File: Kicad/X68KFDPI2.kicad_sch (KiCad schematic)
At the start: 29 parts, among them J1 HxC Connector, J11 Micro_SD_Card, J13 FD Int/Ext (0,1/2,3), J2 FD Ext Connector, J3 FD00, J4 FD01, J7 LedFD0, J8 LedFD1, J9 FloppyPWR, SW1 SW_Push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

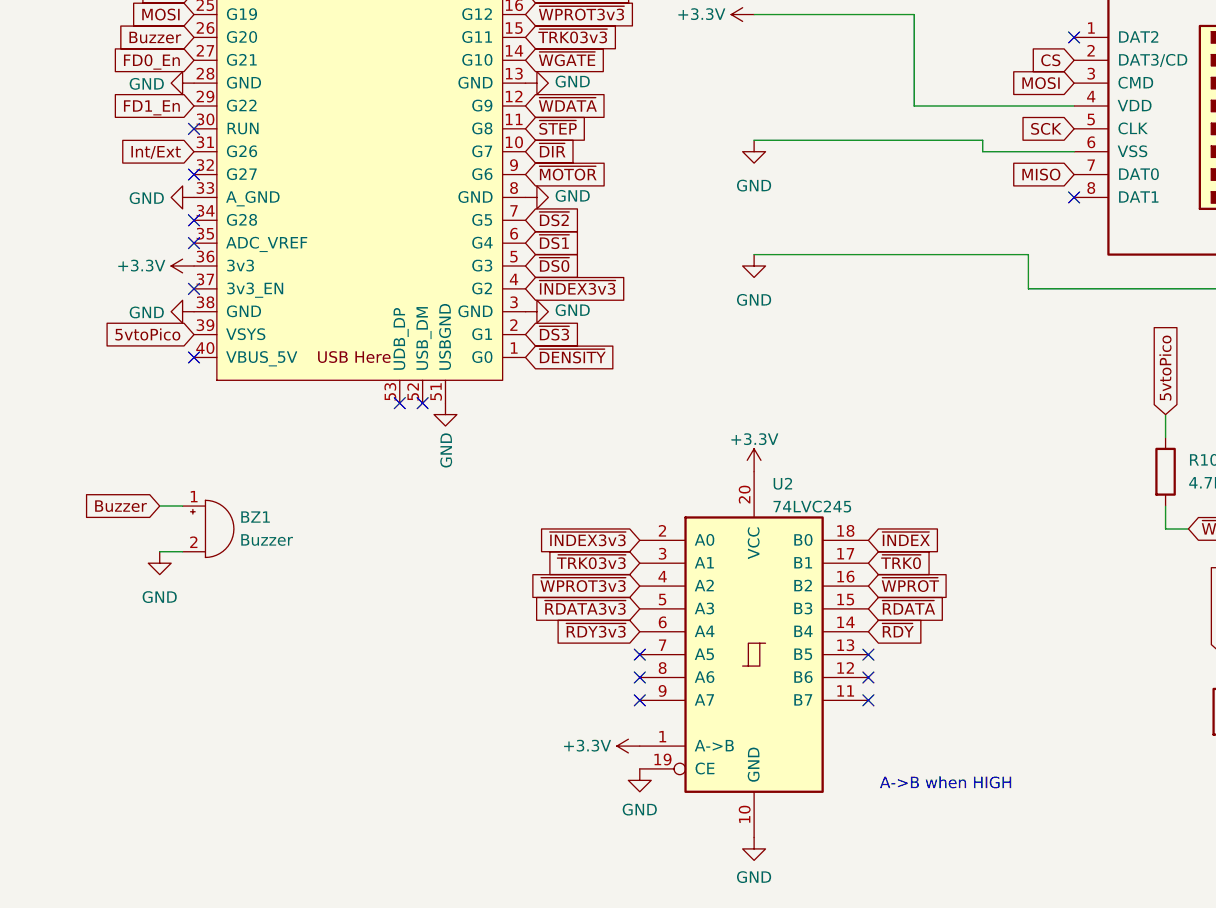
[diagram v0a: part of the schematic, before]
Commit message: Added 74lvc245 dir control
Test in progress for avoiding conflict when 2 x68kfdpi2w are used togheter
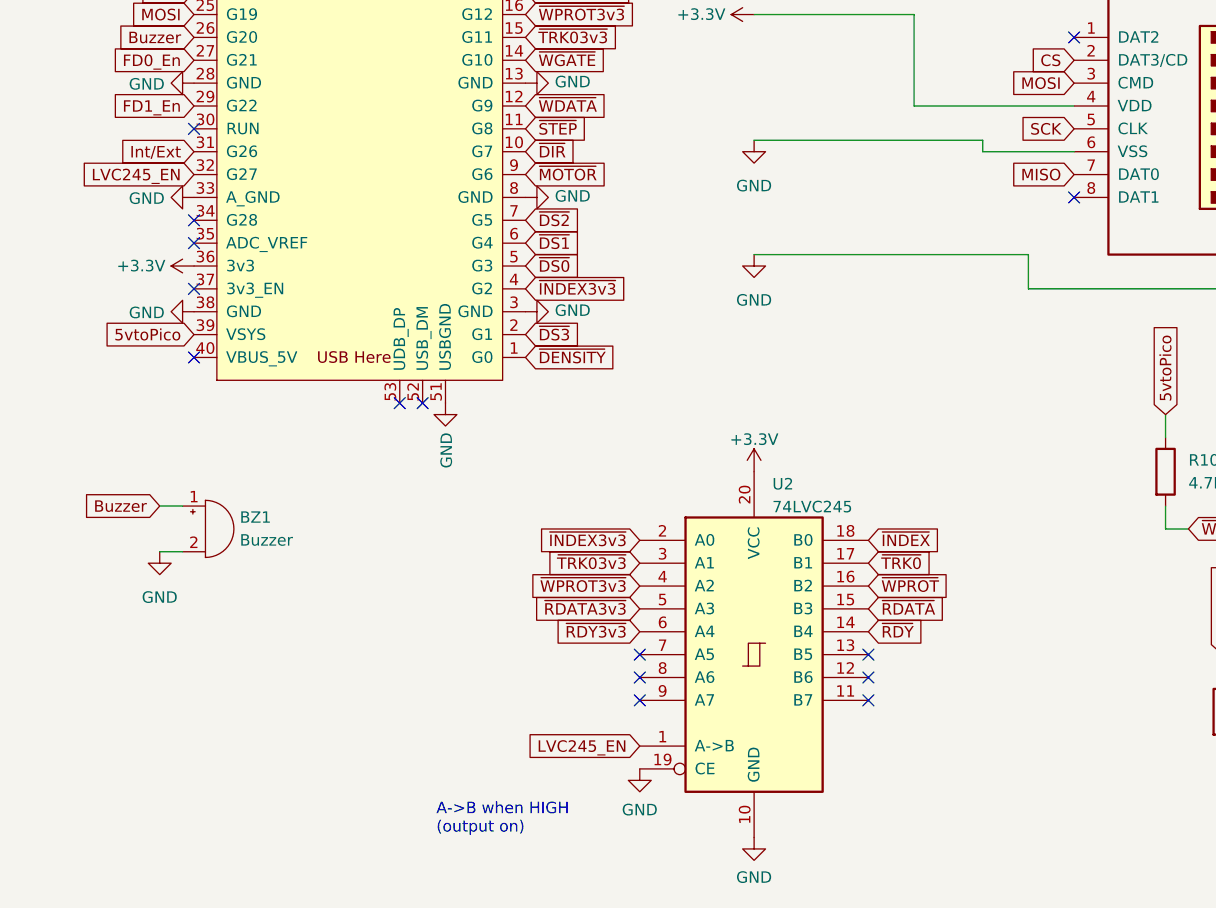
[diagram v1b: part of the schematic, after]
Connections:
- net +3.3V: no longer U2.1 (A->B)
- net LVC245_EN: now reaches RP1.32 (G27)
- net LVC245_EN: now also U2.1 (A->B)
- no-connect marks 31 -> 30
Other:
- note added: "A->B when HIGH (output on)"
- note removed: "A->B when HIGH"
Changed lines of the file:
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@@
 	(generator_version "9.0")
 	(paper "A4")
-	(text "A->B when HIGH"
+	(text "A->B when HIGH \n(output on)"
 		(exclude_from_sim no)
-		(at 105.41 177.8 0)
+		(at 56.134 182.626 0)
 		(effects
 			(font
@@
 	)
 	(no_connect
-		(at 29.21 109.22)
-	)
-	(no_connect
 		(at 29.21 104.14)
 	)
@@
 		)
 	)
+	(global_label "LVC245_EN"
+		(shape input)
+		(at 78.74 172.72 180)
+		(fields_autoplaced yes)
+		(effects
+			(font
+				(size 1.27 1.27)
+			)
+			(justify right)
+		)
+		(property "Intersheetrefs" "${INTERSHEET_REFS}"
+			(at 65.2925 172.72 0)
+			(effects
+				(font
+					(size 1.27 1.27)
+				)
+				(justify right)
+				(hide yes)
+			)
+		)
+	)
 	(global_label "~{MOTOR}"
 		(shape input)
@@
 		)
 	)
+	(global_label "LVC245_EN"
+		(shape input)
+		(at 29.21 109.22 180)
+		(fields_autoplaced yes)
+		(effects
+			(font
+				(size 1.27 1.27)
+			)
+			(justify right)
+		)
+		(property "Intersheetrefs" "${INTERSHEET_REFS}"
+			(at 15.7625 109.22 0)
+			(effects
+				(font
+					(size 1.27 1.27)
+				)
+				(justify right)
+				(hide yes)
+			)
+		)
+	)
 	(global_label "LEDFD0"
 		(shape input)
@@
 					(unit 1)
 				)
-			)
-		)
-	)
-	(symbol
-		(lib_id "power:+3.3V")
-		(at 78.74 172.72 90)
-		(unit 1)
-		(exclude_from_sim no)
-		(in_bom yes)
-		(on_board yes)
-		(dnp no)
-		(fields_autoplaced yes)
-		(property "Reference" "#PWR041"
-			(at 82.55 172.72 0)
-			(effects
-				(font
-					(size 1.27 1.27)
-				)
-				(hide yes)
-			)
-		)
-		(property "Value" "+3.3V"
-			(at 75.565 172.72 90)
-			(effects
-				(font
-					(size 1.27 1.27)
-				)
-				(justify left)
-			)
-		)
-		(property "Footprint" ""
-			(at 78.74 172.72 0)
-			(effects
-				(font
-					(size 1.27 1.27)
-				)
-				(hide yes)
-			)
-		)
-		(property "Datasheet" ""
-			(at 78.74 172.72 0)
-			(effects
-				(font
-					(size 1.27 1.27)
-				)
-				(hide yes)
-			)
-		)
-		(property "Description" "Power symbol creates a global label with name \"+3.3V\""
-			(at 78.74 172.72 0)
-			(effects
-				(font
-					(size 1.27 1.27)
-				)
-				(hide yes)
-			)
-		)
-		(pin "1"
-		)
-		(instances
-			(project "X68KFDPI2"
-				(path "/0f251f4d-18c3-4e16-8078-b8eaa683a5b6"
-					(reference "#PWR041")
-					(unit 1)
-				)

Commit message: Fix for drive 0/1-2/3
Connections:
- net +3.3V: now also J13.3 (Pin_3), U1.36 (3V3)
- net 5vtoPico: no longer J13.3 (Pin_3)
- no-connect marks 30 -> 29
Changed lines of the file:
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@@
 	)
 	(no_connect
-		(at 152.4 33.02)
-	)
-	(no_connect
 		(at 198.12 25.4)
 	)
@@
 		)
 	)
-	(global_label "5vtoPico"
-		(shape input)
-		(at 171.45 38.1 270)
-		(fields_autoplaced yes)
-		(effects
-			(font
-				(size 1.27 1.27)
-			)
-			(justify right)
-		)
-		(property "Intersheetrefs" "${INTERSHEET_REFS}"
-			(at 171.45 49.2494 90)
-			(effects
-				(font
-					(size 1.27 1.27)
-				)
-				(justify right)
-				(hide yes)
-			)
-		)
-	)
 	(global_label "~{OPT2}"
 		(shape input)
@@
 	)
 	(symbol
+		(lib_id "power:+3.3V")
+		(at 171.45 38.1 180)
+		(unit 1)
+		(exclude_from_sim no)
+		(in_bom yes)
+		(on_board yes)
+		(dnp no)
+		(fields_autoplaced yes)
+		(property "Reference" "#PWR021"
+			(at 171.45 34.29 0)
+			(effects
+				(font
+					(size 1.27 1.27)
+				)
+				(hide yes)
+			)
+		)
+		(property "Value" "+3.3V"
+			(at 171.45 43.18 0)
+			(effects
+				(font
+					(size 1.27 1.27)
+				)
+			)
+		)
+		(property "Footprint" ""
+			(at 171.45 38.1 0)
+			(effects
+				(font
+					(size 1.27 1.27)
+				)
+				(hide yes)
+			)
+		)
+		(property "Datasheet" ""
+			(at 171.45 38.1 0)
+			(effects
+				(font
+					(size 1.27 1.27)
+				)
+				(hide yes)
+			)
+		)
+		(property "Description" "Power symbol creates a global label with name \"+3.3V\""
+			(at 171.45 38.1 0)
+			(effects
+				(font
+					(size 1.27 1.27)
+				)
+				(hide yes)
+			)
+		)
+		(pin "1"
+		)
+		(instances
+			(project "X68KFDPI2"
+				(path "/0f251f4d-18c3-4e16-8078-b8eaa683a5b6"
+					(reference "#PWR021")
+					(unit 1)
+				)
+			)
+		)
+	)
+	(symbol
 		(lib_id "74xx:74LS245")
 		(at 91.44 162.56 0)
@@
 					(unit 1)
 				)
+			)
+		)
+	)
+	(symbol
+		(lib_id "power:+3.3V")
+		(at 152.4 33.02 180)
+		(unit 1)
+		(exclude_from_sim no)
+		(in_bom yes)
+		(on_board yes)
+		(dnp no)
+		(fields_autoplaced yes)
+		(property "Reference" "#PWR013"
+			(at 152.4 29.21 0)
+			(effects
+				(font
+					(size 1.27 1.27)
+				)
+				(hide yes)
+			)
+		)
+		(property "Value" "+3.3V"
+			(at 152.4 38.1 0)
+			(effects
+				(font
+					(size 1.27 1.27)
+				)
+			)
+		)
+		(property "Footprint" ""
+			(at 152.4 33.02 0)
+			(effects
+				(font
+					(size 1.27 1.27)
+				)
+				(hide yes)
+			)
+		)
+		(property "Datasheet" ""
+			(at 152.4 33.02 0)
+			(effects
+				(font
+					(size 1.27 1.27)
+				)
+				(hide yes)
+			)
+		)
+		(property "Description" "Power symbol creates a global label with name \"+3.3V\""
+			(at 152.4 33.02 0)
+			(effects
+				(font
+					(size 1.27 1.27)
+				)
+				(hide yes)
+			)
+		)
+		(pin "1"
+		)
+		(instances
+			(project ""
+				(path "/0f251f4d-18c3-4e16-8078-b8eaa683a5b6"
+					(reference "#PWR013")
+					(unit 1)
+				)

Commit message: Fixed fdd power connector
Fixed 5vsb to gnd in fdd power connector for some models
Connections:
- net GND: no longer J9.3 (Pin_3)
- no-connect marks 29 -> 30
